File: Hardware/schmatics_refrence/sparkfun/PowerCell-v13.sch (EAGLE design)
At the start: 28 parts, among them IC1 MC33269D-3.3, U1 MCP73831, U2 TPS61200, X1 USB-MICROB

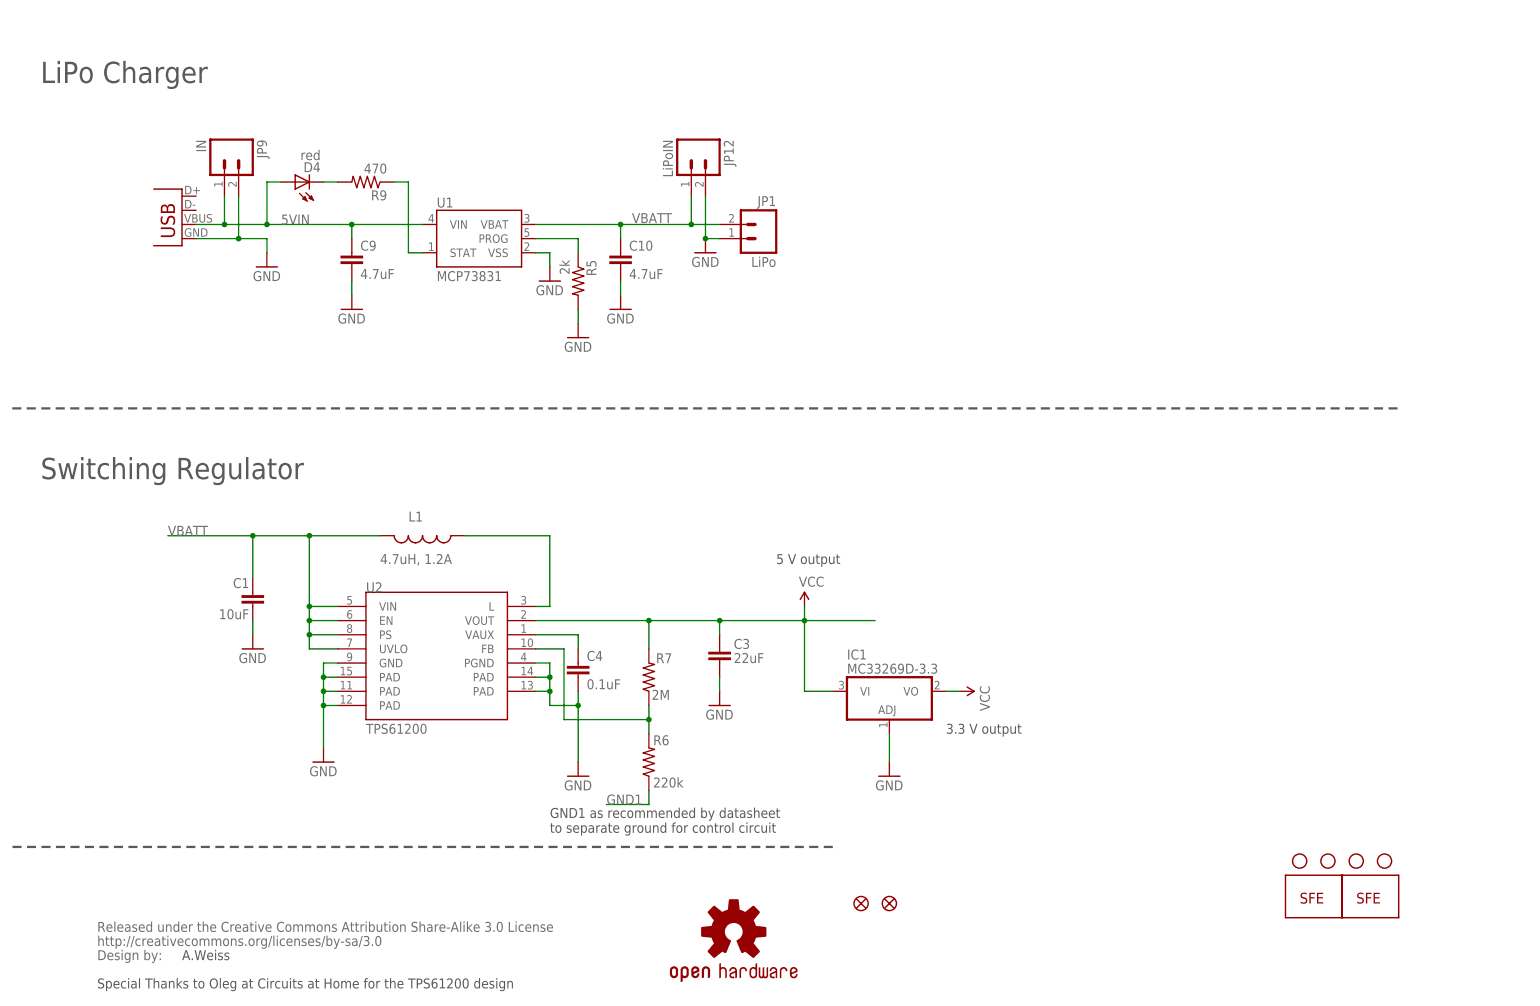
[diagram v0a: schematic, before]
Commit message: + Lots of changes and corrections - Does not meet DRC Yet - Still need to implement option to swap out power supplies from 9V battery to LiOn
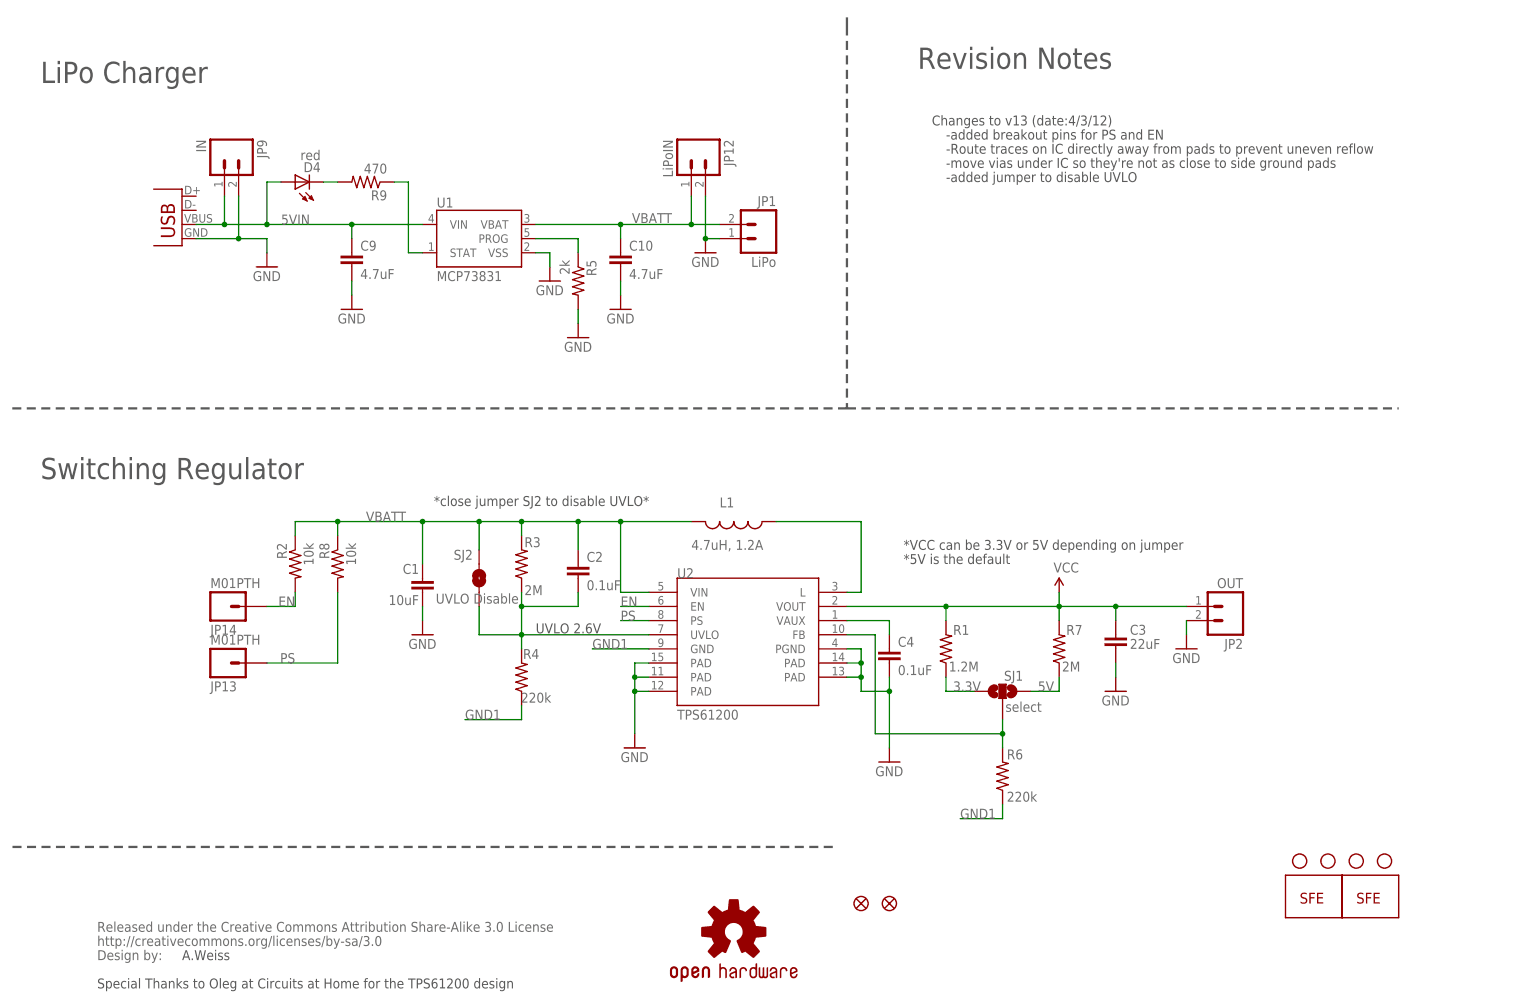
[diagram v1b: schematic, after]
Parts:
- removed IC1: MC33269D-3.3, linear:MC33269D-3.3
- added C2: 0.1uF, SparkFun:CAP0402-CAP
- added JP13, JP14: M01PTH, SparkFun:M01PTH
- added JP2: OUT, SparkFun:M02PTH
- added R1: 1.2M, SparkFun:RESISTOR0402-RES
- added R2, R8: 10k, SparkFun:RESISTOR0402-RES
- added R3: 2M, SparkFun:RESISTOR0402-RES
- added R4: 220k, SparkFun:RESISTOR0402-RES
- added SJ1: select, SparkFun:SOLDERJUMPER_2WAYPASTE2&3
- added SJ2: UVLO Disable, SparkFun-Passives:SOLDERJUMPERNO
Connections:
- new net 3.3V: R1.1, SJ1.1
- new net 5V: R7.1, SJ1.3
- new net EN: JP14.1, R2.2, U2.EN
- new net PS: JP13.1, R8.2, U2.PS
- new net UVLO: C2.2, R3.1, R4.2, SJ2.1, U2.UVLO
- net FB: now also SJ1.2; no longer R7.1
- net GND: now also JP2.2; no longer IC1.ADJ, U2.GND
- net GND1: now also R4.1, U2.GND
- net VBATT: now also C2.1, R2.1, R3.2, R8.1, SJ2.2; no longer U2.EN, U2.PS, U2.UVLO
- net VCC: now also JP2.1, R1.2; no longer IC1.VI, IC1.VO
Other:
- note added: "*5V is the default"
- note added: "*VCC can be 3.3V or 5V depending on jumper"
- note added: "*close jumper SJ2 to disable UVLO*"
- note added: "-Route traces on IC directly away from pads to prevent uneven reflow"
- note added: "-added breakout pins for PS and EN"
- note added: "-added jumper to disable UVLO"
- note added: "-move vias under IC so they're not as close to side ground pads"
- note added: "Changes to v13 (date:4/3/12)"
- note added: "Revision Notes"
- note added: "UVLO 2.6V"
- note removed: "3.3 V output"
- note removed: "5 V output"
- note removed: "GND1 as recommended by datasheet to separate ground for control circuit"
- moved on the sheet: C1, C3, C4, L1, R6, R7, U2
